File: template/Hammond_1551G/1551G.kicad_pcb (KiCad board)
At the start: 2 copper layers, 44.5 x 29.5 mm, 2 parts

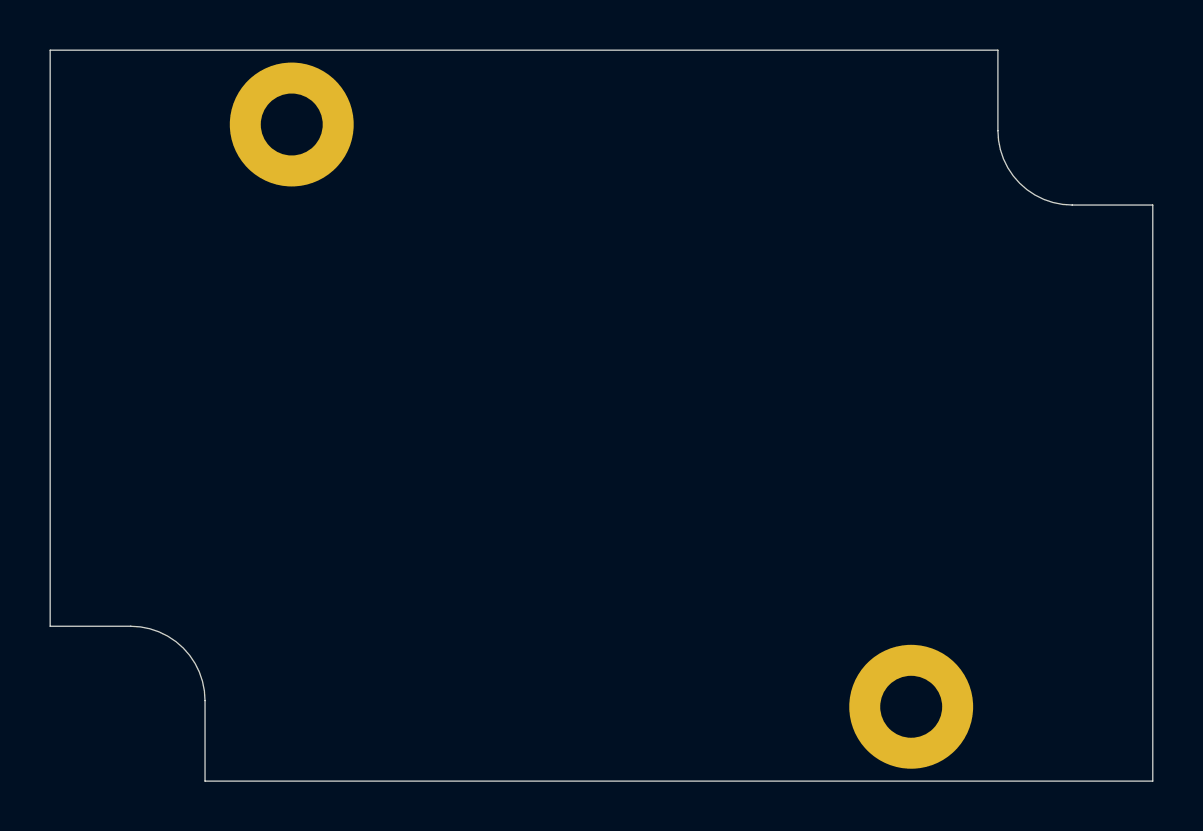
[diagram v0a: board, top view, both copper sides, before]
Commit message: feat: Add Templates for Hammond Enclosures
add templates for 1551

Issue #17
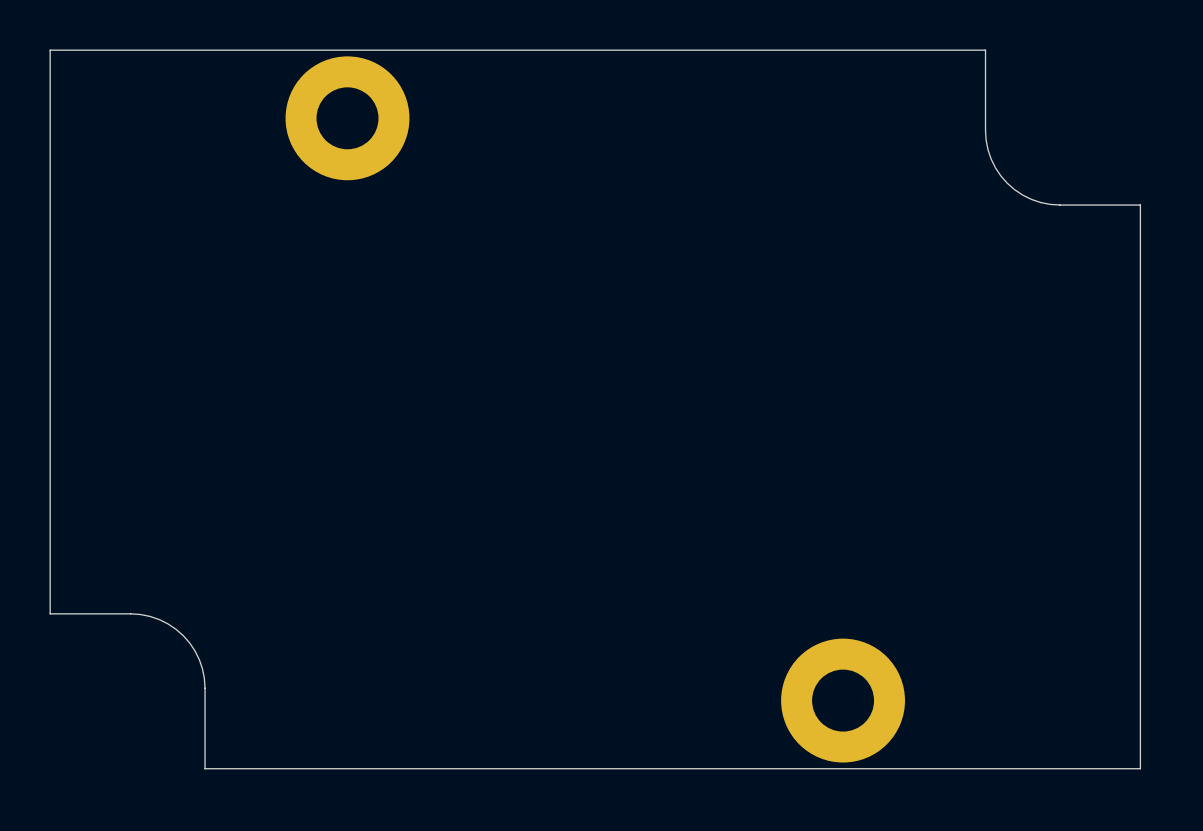
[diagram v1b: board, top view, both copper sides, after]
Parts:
- moved ~ 2.76 mm to (47.0, 41.2)
- moved ~ 2.26 mm to (27.0, 17.8)
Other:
- board size 44.5 x 29.5 mm -> 44 x 29 mm
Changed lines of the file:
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@@
     (pad_to_mask_clearance 0.051)
     (solder_mask_min_width 0.25)
-    (aux_axis_origin 15 44.5)
+    (aux_axis_origin 15 44)
     (visible_elements 7FFFFFFF)
     (pcbplotparams
@@
   )
   (module MountingHole:MountingHole_2.5mm_Pad (layer F.Cu)
-    (at 49.75 41.5)
+    (at 47 41.25)
     (descr "Mounting Hole 2.5mm")
     (tags "mounting hole 2.5mm")
@@
   )
   (module MountingHole:MountingHole_2.5mm_Pad (layer F.Cu)
-    (at 24.75 18)
+    (at 27 17.75)
     (descr "Mounting Hole 2.5mm")
     (tags "mounting hole 2.5mm")
@@
     (pad 1 thru_hole circle (at 0 0) (size 5 5) (drill 2.5) (layers *.Cu *.Mask))
   )
-  (gr_line (start 18.25 38.25) (end 15 38.25) (layer Edge.Cuts) (width 0.05))
-  (gr_line (start 21.25 44.5) (end 21.25 41.25) (layer Edge.Cuts) (width 0.05))
-  (gr_line (start 56.25 21.25) (end 59.5 21.25) (layer Edge.Cuts) (width 0.05))
-  (gr_line (start 53.25 18.25) (end 53.25 15) (layer Edge.Cuts) (width 0.05))
-  (gr_arc (start 56.25 18.25) (end 53.25 18.25) (angle -90) (layer Edge.Cuts) (width 0.05))
-  (gr_arc (start 18.25 41.25) (end 21.25 41.25) (angle -90) (layer Edge.Cuts) (width 0.05))
-  (dimension 44.5 (width 0.15) (layer Dwgs.User)
-    (gr_text "44.500 mm" (at 37.25 49.8) (layer Dwgs.User)
+  (dimension 44 (width 0.15) (layer Dwgs.User)
+    (gr_text "44,000 mm" (at 37 50.3) (layer Dwgs.User)
       (effects (font (size 1 1) (thickness 0.15)))
     )
-    (feature1 (pts (xy 15 44.5) (xy 15 49.086421)))
-    (feature2 (pts (xy 59.5 44.5) (xy 59.5 49.086421)))
-    (crossbar (pts (xy 59.5 48.5) (xy 15 48.5)))
-    (arrow1a (pts (xy 15 48.5) (xy 16.126504 47.913579)))
-    (arrow1b (pts (xy 15 48.5) (xy 16.126504 49.086421)))
-    (arrow2a (pts (xy 59.5 48.5) (xy 58.373496 47.913579)))
-    (arrow2b (pts (xy 59.5 48.5) (xy 58.373496 49.086421)))
+    (feature1 (pts (xy 15 44) (xy 15 49.586421)))
+    (feature2 (pts (xy 59 44) (xy 59 49.586421)))
+    (crossbar (pts (xy 59 49) (xy 15 49)))
+    (arrow1a (pts (xy 15 49) (xy 16.126504 48.413579)))
+    (arrow1b (pts (xy 15 49) (xy 16.126504 49.586421)))
+    (arrow2a (pts (xy 59 49) (xy 57.873496 48.413579)))
+    (arrow2b (pts (xy 59 49) (xy 57.873496 49.586421)))
   )
-  (dimension 29.5 (width 0.15) (layer Dwgs.User)
-    (gr_text "29.500 mm" (at 65.8 29.75 270) (layer Dwgs.User)
+  (dimension 29 (width 0.15) (layer Dwgs.User)
+    (gr_text "29,000 mm" (at 65.3 29.5 270) (layer Dwgs.User)
       (effects (font (size 1 1) (thickness 0.15)))
     )
-    (feature1 (pts (xy 59.5 44.5) (xy 65.086421 44.5)))
-    (feature2 (pts (xy 59.5 15) (xy 65.086421 15)))
-    (crossbar (pts (xy 64.5 15) (xy 64.5 44.5)))
-    (arrow1a (pts (xy 64.5 44.5) (xy 63.913579 43.373496)))
-    (arrow1b (pts (xy 64.5 44.5) (xy 65.086421 43.373496)))
-    (arrow2a (pts (xy 64.5 15) (xy 63.913579 16.126504)))
-    (arrow2b (pts (xy 64.5 15) (xy 65.086421 16.126504)))
+    (feature1 (pts (xy 59 44) (xy 64.586421 44)))
+    (feature2 (pts (xy 59 15) (xy 64.586421 15)))
+    (crossbar (pts (xy 64 15) (xy 64 44)))
+    (arrow1a (pts (xy 64 44) (xy 63.413579 42.873496)))
+    (arrow1b (pts (xy 64 44) (xy 64.586421 42.873496)))
+    (arrow2a (pts (xy 64 15) (xy 63.413579 16.126504)))
+    (arrow2b (pts (xy 64 15) (xy 64.586421 16.126504)))
   )
-  (gr_line (start 21.25 44.5) (end 59.5 44.5) (layer Edge.Cuts) (width 0.05))
-  (gr_line (start 59.5 21.25) (end 59.5 44.5) (layer Edge.Cuts) (width 0.05))
-  (gr_line (start 15 15) (end 15 38.25) (layer Edge.Cuts) (width 0.05))
-  (gr_line (start 15 15) (end 53.25 15) (layer Edge.Cuts) (width 0.05))
+  (gr_line (start 52.75 18.25) (end 52.75 15) (layer Edge.Cuts) (width 0.05))
+  (gr_line (start 55.75 21.25) (end 59 21.25) (layer Edge.Cuts) (width 0.05))
+  (gr_line (start 21.25 40.75) (end 21.25 44) (layer Edge.Cuts) (width 0.05))
+  (gr_line (start 18.25 37.75) (end 15 37.75) (layer Edge.Cuts) (width 0.05))
+  (gr_arc (start 18.25 40.75) (end 21.25 40.75) (angle -90) (layer Edge.Cuts) (width 0.05))
+  (gr_arc (start 55.75 18.25) (end 52.75 18.25) (angle -90) (layer Edge.Cuts) (width 0.05))
+  (gr_line (start 15 37.75) (end 15 15) (layer Edge.Cuts) (width 0.05))
+  (gr_line (start 59 44) (end 21.25 44) (layer Edge.Cuts) (width 0.05))
+  (gr_line (start 59 21.25) (end 59 44) (layer Edge.Cuts) (width 0.05))
+  (gr_line (start 15 15) (end 52.75 15) (layer Edge.Cuts) (width 0.05))
 )
